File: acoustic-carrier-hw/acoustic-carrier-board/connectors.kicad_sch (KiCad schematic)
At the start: 2 parts, among them J704 PMOD_GPIO, J903 Conn_02x06_Odd_Even

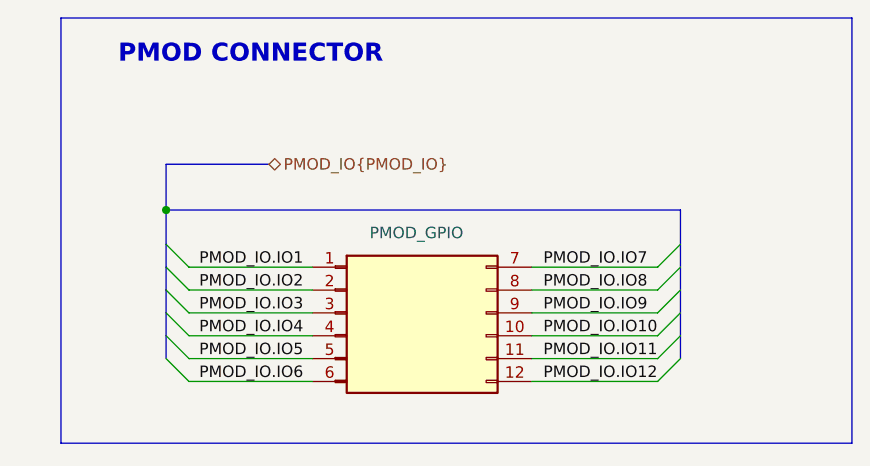
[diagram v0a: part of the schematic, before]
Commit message: [carrier] finished for production (next) reroute the LPDDR3, with appropriate CMD-CTRL bus delays, and change banks for command-control
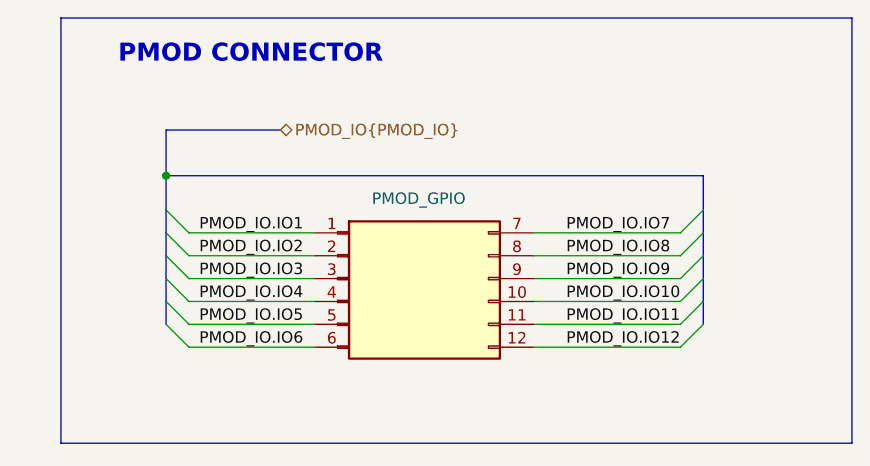
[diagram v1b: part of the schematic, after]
